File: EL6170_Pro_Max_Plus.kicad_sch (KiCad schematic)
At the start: 56 parts, among them J1 USB_C_Receptacle, Q1 MMBT3904, Q2 MMBT3904, SW1 RST, SW2 BOOT, U1 ESP32-S3, U3 ESP-PSRAM64H, U4 W25Q128JVS, U5 ME6217C33M5, U6 CH340K, U7 RFANT5220110A0T, U8 CH334R, X1 40MHz, X2 12MHz

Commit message: sync
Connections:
- net VDD is gone; now on net +3V3: C1.1, C2.1, SH1.8 (VDD)
- net VPP renamed 12VPP
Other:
- moved on the sheet: C1, C2, C3, C4, C5, C6, C7, R1, SH1

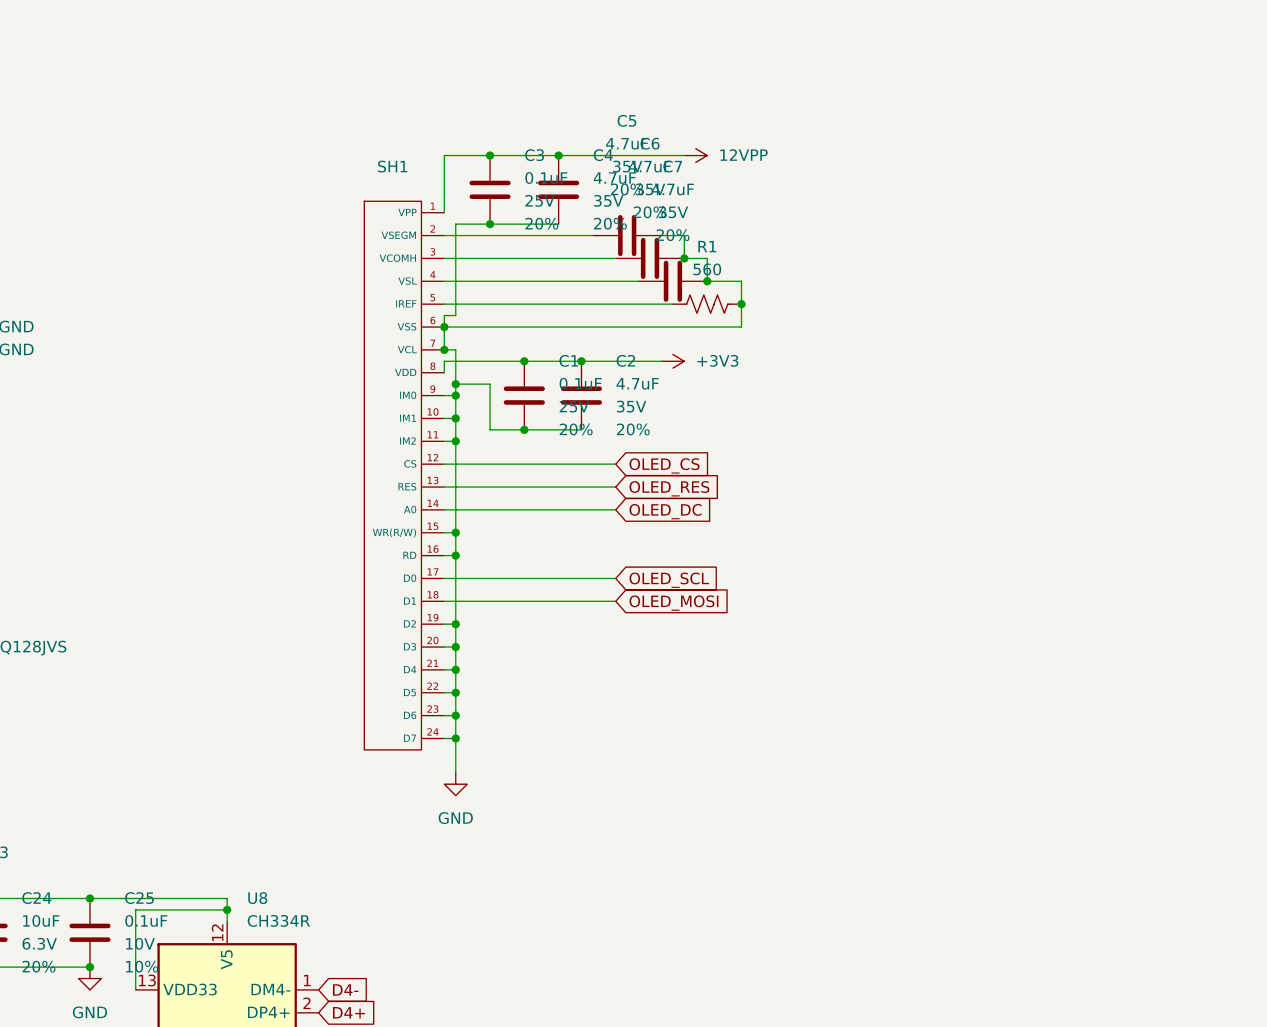
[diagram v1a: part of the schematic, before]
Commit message: add TPS61040DBV
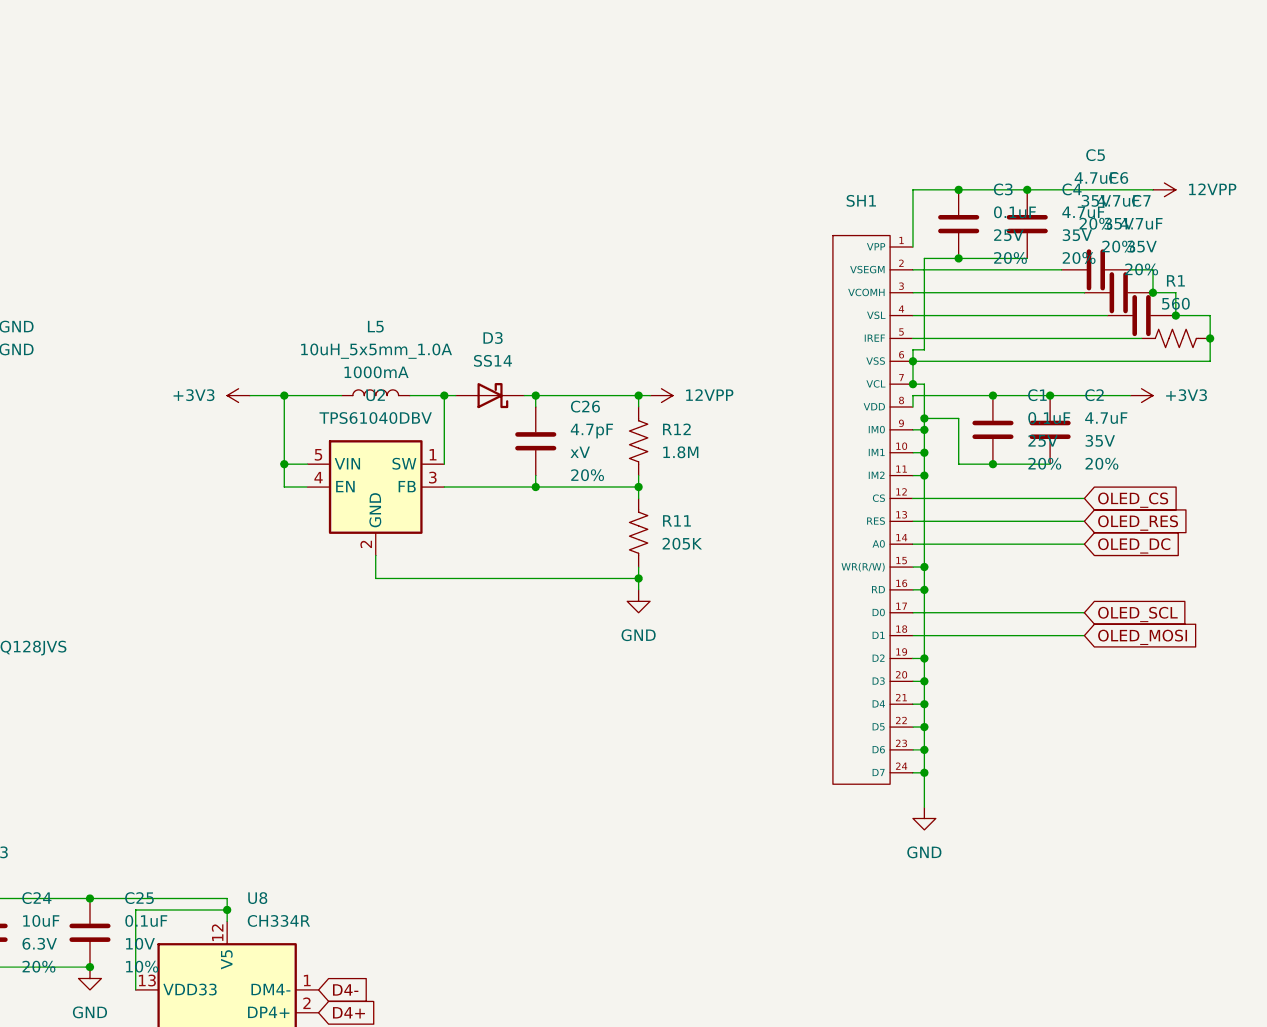
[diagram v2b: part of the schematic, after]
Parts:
- added C26: 4.7pF, SparkFun-Capacitor:C_0402_1005Metric, symbol SparkFun-Capacitor:4.7uF_0402_6.3V_10%
- added D3: SS14, Diode_SMD:D_SMA, symbol Diode:SS14
- added L5: 10uH_5x5mm_1.0A, SparkFun-Coil:Inductor_4.7x4.7mm, symbol SparkFun-Coil:10uH_5x5mm_1.0A
- added R11: 205K, SparkFun-Resistor:R_0603_1608Metric, symbol SparkFun-Resistor:0_0603
- added R12: 1.8M, SparkFun-Resistor:R_0603_1608Metric, symbol SparkFun-Resistor:0_0603
- added U2: TPS61040DBV, Package_TO_SOT_SMD:SOT-23-5, symbol Regulator_Switching:TPS61040DBV
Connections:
- net +3V3: now also L5.1, U2.4 (EN), U2.5 (VIN)
- net 12VPP: now also C26.2, D3.1 (K), R12.1
- net GND: now also R11.2, U2.2 (GND)
- new net: D3.2 (A), L5.2, U2.1 (SW)
- new net: C26.1, R11.1, R12.2, U2.3 (FB)
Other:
- moved on the sheet: C1, C2, C3, C4, C5, C6, C7, R1, SH1

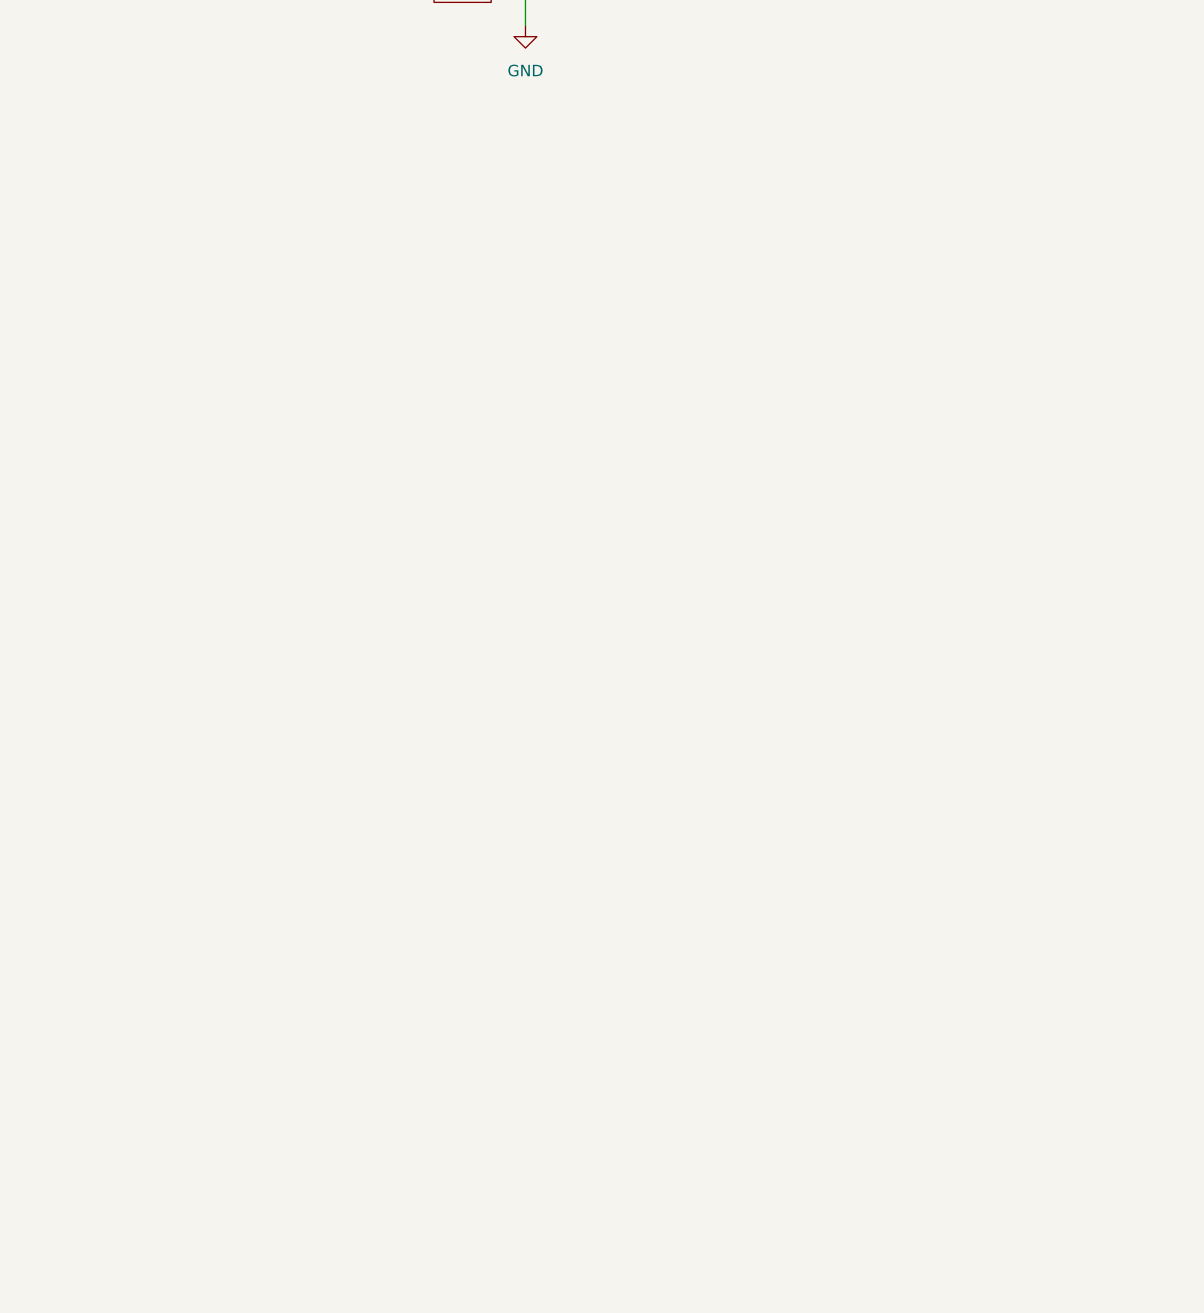
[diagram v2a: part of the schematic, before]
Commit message: add PCM5102A
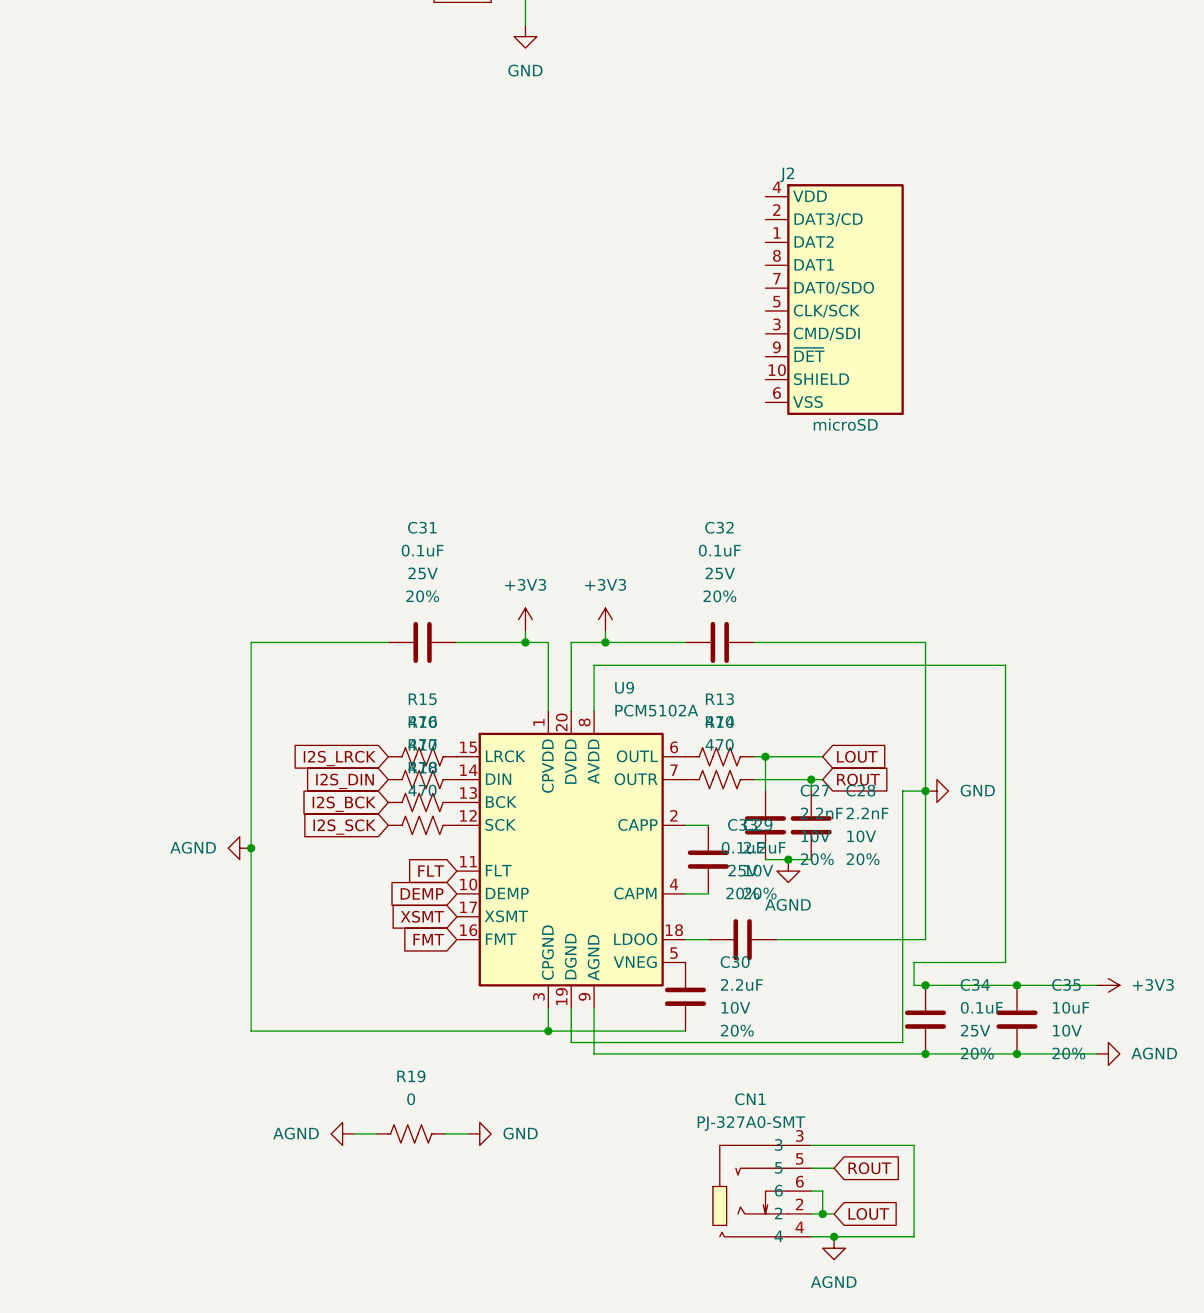
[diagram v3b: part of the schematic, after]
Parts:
- added C27, C28: 2.2nF, SparkFun-Capacitor:C_0603_1608Metric, symbol SparkFun-Capacitor:2.2uF_0603_10V_20%
- added C29, C30: 2.2uF, SparkFun-Capacitor:C_0603_1608Metric, symbol SparkFun-Capacitor:2.2uF_0603_10V_20%
- added C31, C32, C33, C34: 0.1uF, SparkFun-Capacitor:C_0603_1608Metric, symbol SparkFun-Capacitor:0.1uF_0603_25V_20%
- added C35: 10uF, SparkFun-Capacitor:C_0603_1608Metric, symbol SparkFun-Capacitor:10uF_0603_10V_20%
- added CN1: PJ-327A0-SMT, easyeda2kicad:AUDIO-SMD_PJ-327A0-SMT, symbol easyeda2kicad:PJ-327A0-SMT
- added J2: microSD, SparkFun-Connector:microSD_External_Pin, symbol SparkFun-Connector:microSD_PushPush
- added R13, R14, R15, R16, R17, R18: 470, SparkFun-Resistor:R_0603_1608Metric, symbol SparkFun-Resistor:470_0603
- added R19: 0, SparkFun-Resistor:R_0603_1608Metric, symbol SparkFun-Resistor:0_0603
- added U9: PCM5102A, Package_SO:TSSOP-20_4.4x6.5mm_P0.65mm, symbol Audio:PCM5102A
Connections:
- net +3V3: now also C31.2, C32.1, C34.2, C35.1, U9.1 (CPVDD), U9.20 (DVDD), U9.8 (AVDD)
- net GND: now also C32.2, C33.2, R19.1, U9.19 (DGND)
- new net: C30.1, U9.5 (VNEG)
- new net: R13.2, U9.6 (OUTL)
- new net: R16.1, U9.14 (DIN)
- new net: R17.1, U9.13 (BCK)
- new net: C33.1, U9.18 (LDOO)
- new net: R18.1, U9.12 (SCK)
- new net: R15.1, U9.15 (LRCK)
- new net: C29.1, U9.2 (CAPP)
- new net: C29.2, U9.4 (CAPM)
- new net: R14.2, U9.7 (OUTR)
- new net AGND: C27.2, C28.2, C30.2, C31.1, C34.1, C35.2, CN1.3, CN1.4, R19.2, U9.3 (CPGND), U9.9 (AGND)
- new net DEMP: U9.10 (DEMP)
- new net FLT: U9.11 (FLT)
- new net FMT: U9.16 (FMT)
- new net I2S_BCK: R17.2
- new net I2S_DIN: R16.2
- new net I2S_LRCK: R15.2
- new net I2S_SCK: R18.2
- new net LOUT: C27.1, CN1.2, CN1.6, R13.1
- new net ROUT: C28.1, CN1.5, R14.1
- new net XSMT: U9.17 (XSMT)

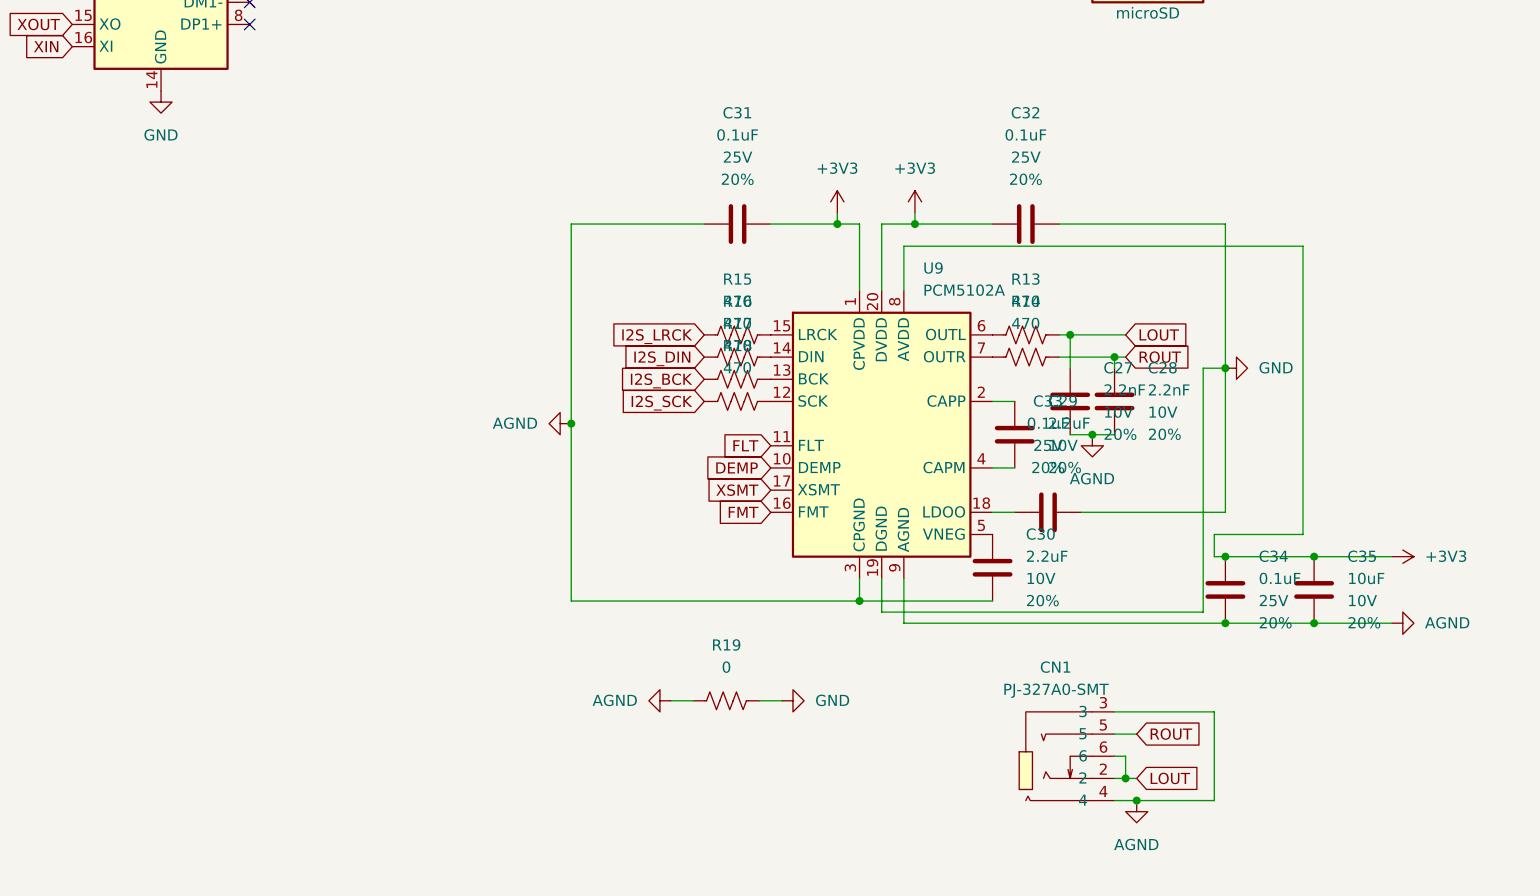
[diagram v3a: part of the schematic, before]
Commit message: add LDO
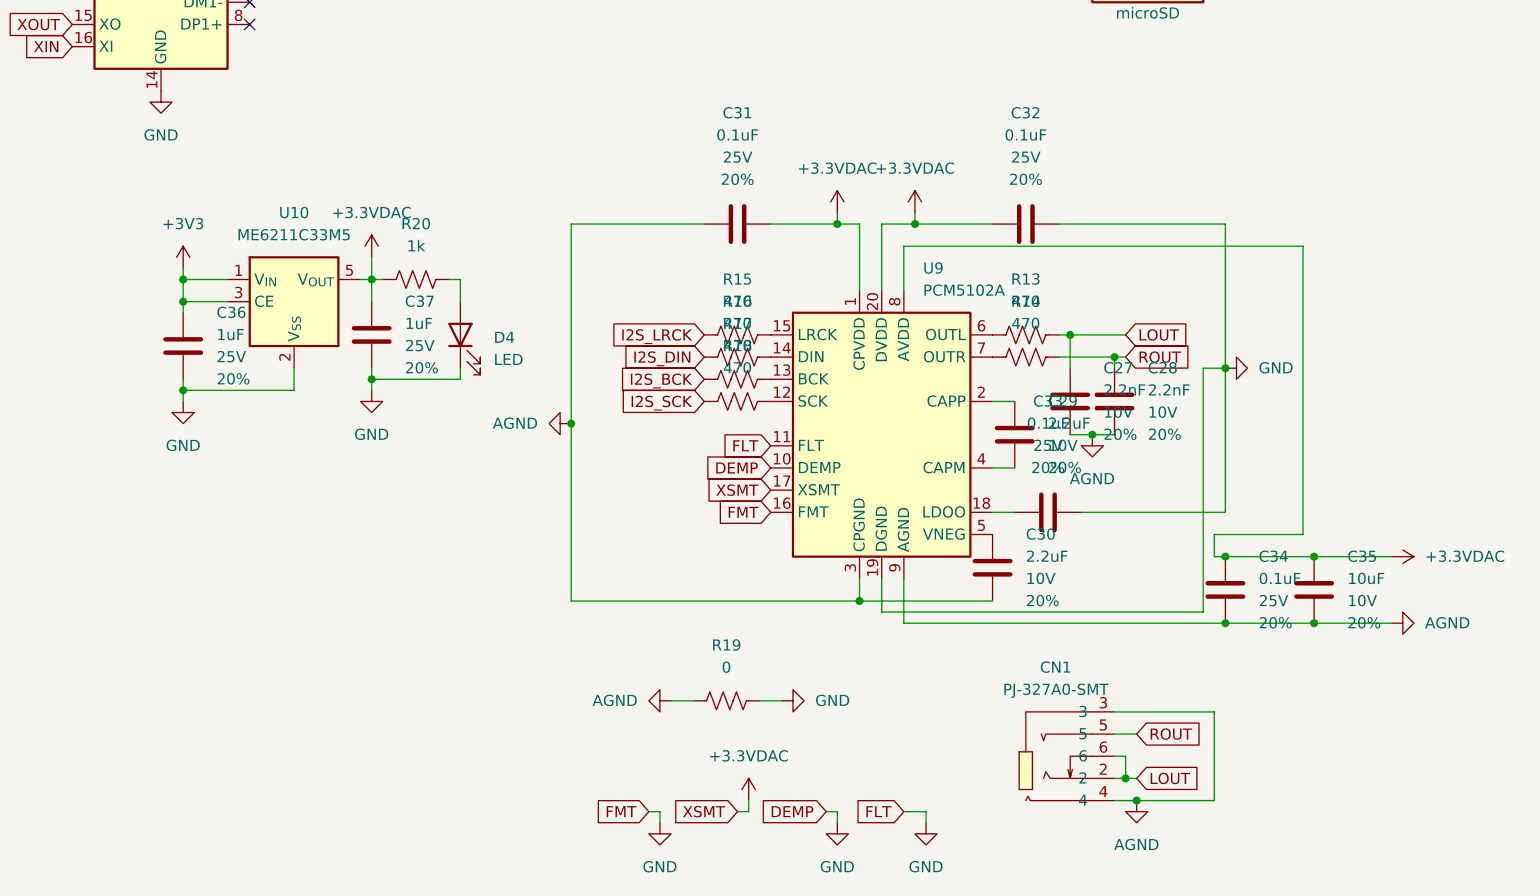
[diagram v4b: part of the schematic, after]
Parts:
- added C36, C37: 1uF, SparkFun-Capacitor:C_0603_1608Metric, symbol SparkFun-Capacitor:0.1uF_0603_25V_20%
- added D4: LED, SparkFun-LED:LED_0603_1608Metric, symbol SparkFun-LED:LED
- added R20: 1k, SparkFun-Resistor:R_0603_1608Metric, symbol SparkFun-Resistor:1k_0603
- added U10: ME6211C33M5, Package_TO_SOT_SMD:SOT-23-5, symbol Regulator_Linear:ME6211C33M5
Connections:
- net DEMP is gone; now on net GND: U9.10 (DEMP)
- net FLT is gone; now on net GND: U9.11 (FLT)
- net FMT is gone; now on net GND: U9.16 (FMT)
- net +3V3: now also C36.1, U10.1 (V_{IN}), U10.3 (CE); no longer C31.2, C32.1, C34.2, C35.1, U9.1 (CPVDD), U9.20 (DVDD), U9.8 (AVDD)
- net GND: now also C36.2, C37.2, D4.1 (K), U10.2 (V_{SS})
- net XSMT renamed +3.3VDAC
- net +3.3VDAC: now also C31.2, C32.1, C34.2, C35.1, U9.1 (CPVDD), U9.20 (DVDD), U9.8 (AVDD), C37.1, R20.2, U10.5 (V_{OUT})
- new net: D4.2 (A), R20.1

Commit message: add IP5306
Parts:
- added U11: IP5306, easyeda2kicad:ESOP-8_L4.9-W3.9-P1.27-LS6.0-BL-EP, symbol easyeda2kicad:IP5306
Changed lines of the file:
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@@
+	)
+	(symbol
+		(lib_id "easyeda2kicad:IP5306")
+		(at 46.99 213.36 0)
+		(unit 1)
+		(exclude_from_sim no)
+		(in_bom yes)
+		(on_board yes)
+		(dnp no)
+		(fields_autoplaced yes)
+		(property "Reference" "U11"
+			(at 46.99 226.06 0)
+			(effects
+				(font
+					(size 1.27 1.27)
+				)
+			)
+		)
+		(property "Value" "IP5306"
+			(at 46.99 228.6 0)
+			(effects
+				(font
+					(size 1.27 1.27)
+				)
+			)
+		)
+		(property "Footprint" "easyeda2kicad:ESOP-8_L4.9-W3.9-P1.27-LS6.0-BL-EP"
+			(at 46.99 228.6 0)
+			(effects
+				(font
+					(size 1.27 1.27)
+				)
+				(hide yes)
+			)
+		)
+		(property "Datasheet" "https://lcsc.com/product-detail/PMIC-Battery-Management_IP5306_C181692.html"
+			(at 46.99 231.14 0)
+			(effects
+				(font
+					(size 1.27 1.27)
+				)
+				(hide yes)
+			)
+		)
+		(property "Description" ""
+			(at 46.99 213.36 0)
+			(effects
+				(font
+					(size 1.27 1.27)
+				)
+				(hide yes)
+			)
+		)
+		(property "LCSC Part" "C181692"
+			(at 46.99 233.68 0)
+			(effects
+				(font
+					(size 1.27 1.27)
+				)
+				(hide yes)
+			)
+		)
+		(pin "1"
+		)
+		(pin "3"
+		)
+		(pin "7"
+		)
+		(pin "8"
+		)
+		(pin "2"
+		)
+		(pin "5"
+		)
+		(pin "6"
+		)
+		(pin "9"
+		)
+		(pin "4"
+		)
+		(instances
+			(project ""
+				(path "/b3287cc9-c0c8-4939-96d8-31efd376f189"
+					(reference "U11")
+					(unit 1)
+				)
+			)
+		)
 	)
 	(symbol
